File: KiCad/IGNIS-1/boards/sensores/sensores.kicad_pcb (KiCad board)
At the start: 2 copper layers, 62 x 62 mm, 16 parts, among them J1 J_PWR_2x4, J41 J_DAT, U20 BME280, U21 MPU6050, U22 MQ-135, U24 GPS NEO-6M

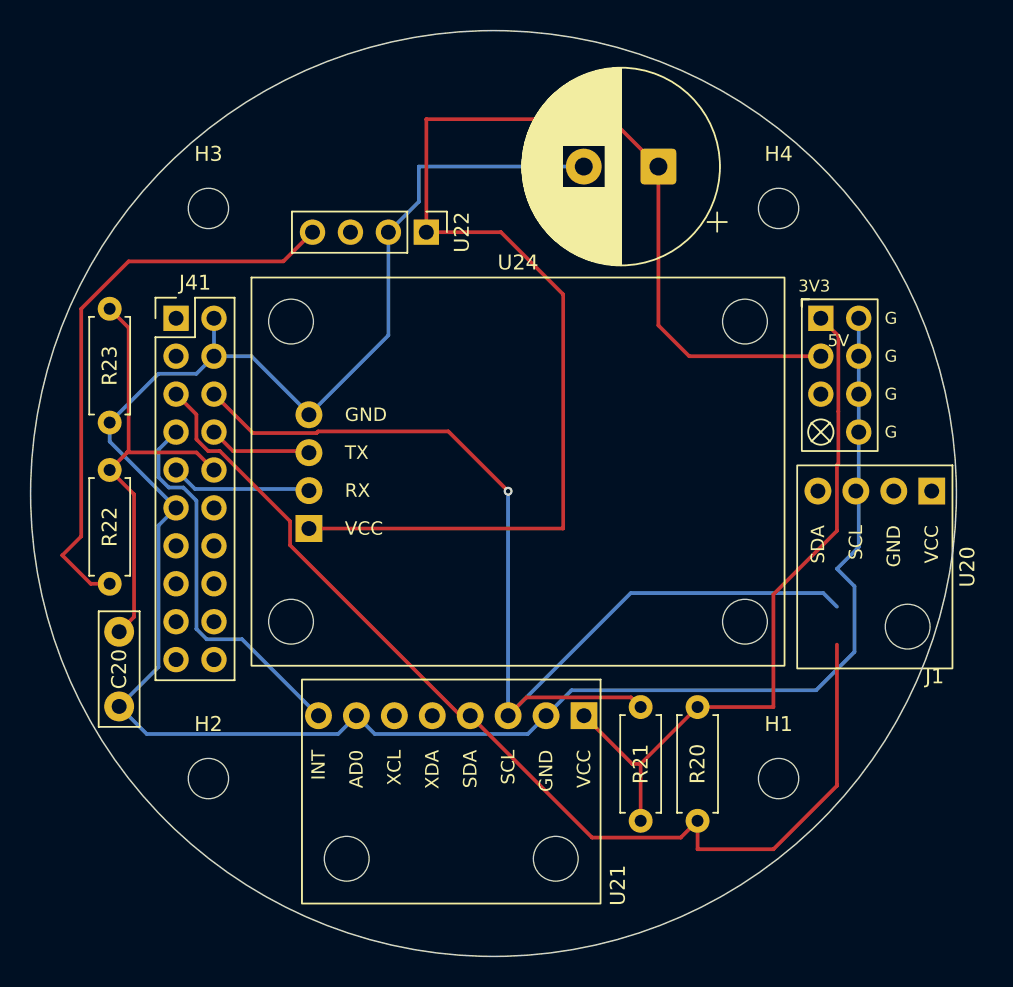
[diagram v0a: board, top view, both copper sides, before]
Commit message: Actualización sensores.kicad_pcb
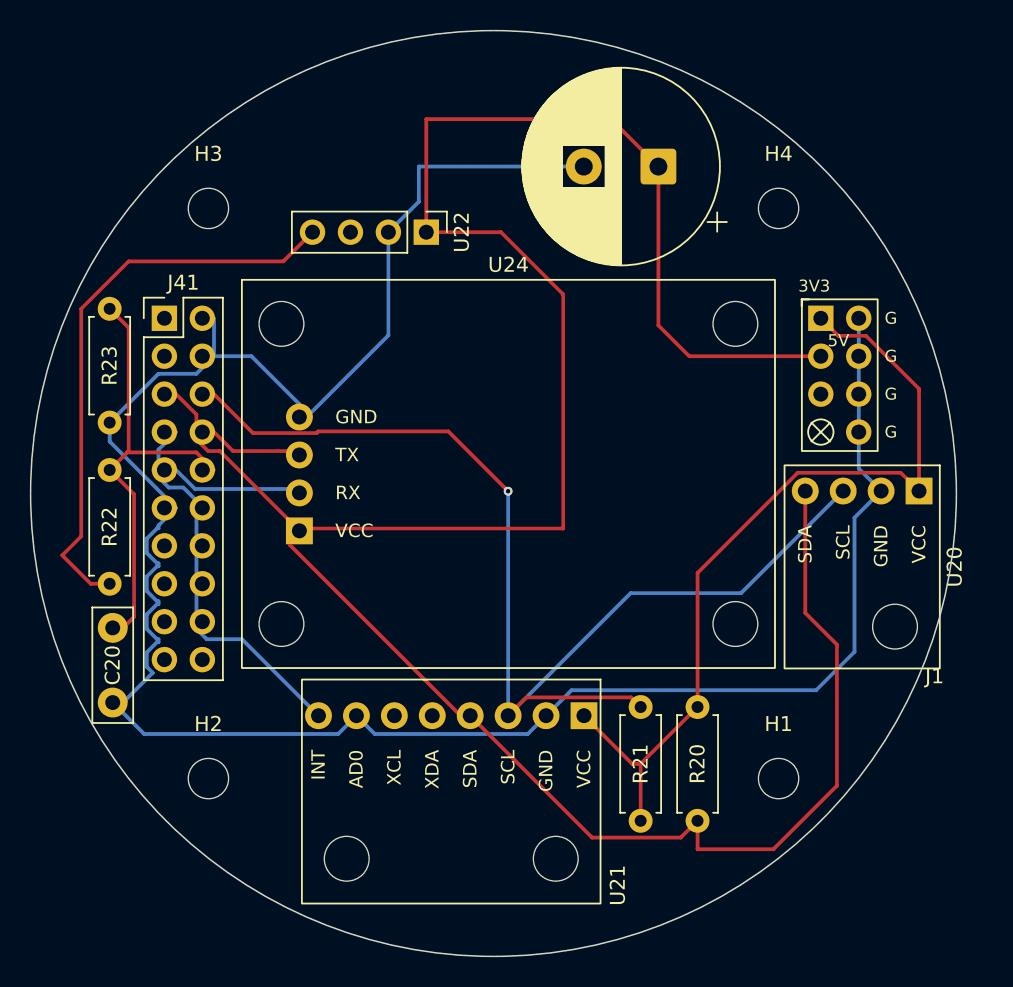
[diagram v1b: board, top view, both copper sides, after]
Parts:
- moved U20 0.85 mm to (124.7, 104.9)
- moved J41 0.78 mm to (78.0, 88.3)
- moved U24 0.66 mm to (101.0, 98.7)
- moved C20 0.50 mm to (74.5, 109.0)
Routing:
- net SDA: track 71.4 -> 82.6 mm
- net +3V3: track 47.7 -> 56.8 mm
- net GND: track 149.1 -> 153.6 mm
- net SCL: track 73.0 -> 75.8 mm

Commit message: Actualización sensores.kicad_pcb
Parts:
- moved U20 0.61 mm to (125.3, 104.9)
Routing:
- net +5V: track 90.4 -> 76.6 mm, vias 0 -> 1
- net SDA: track 82.6 -> 92.9 mm, vias 0 -> 1
- net SCL: track 75.8 -> 79.7 mm
- net MPU_INT: track 25.9 -> 28.5 mm, vias 0 -> 1
- net Net-(U22-A0): track 38.6 -> 37.3 mm
- net MQ_AOUT: track 30.4 -> 29.6 mm
